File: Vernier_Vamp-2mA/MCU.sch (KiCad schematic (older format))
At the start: 9 parts

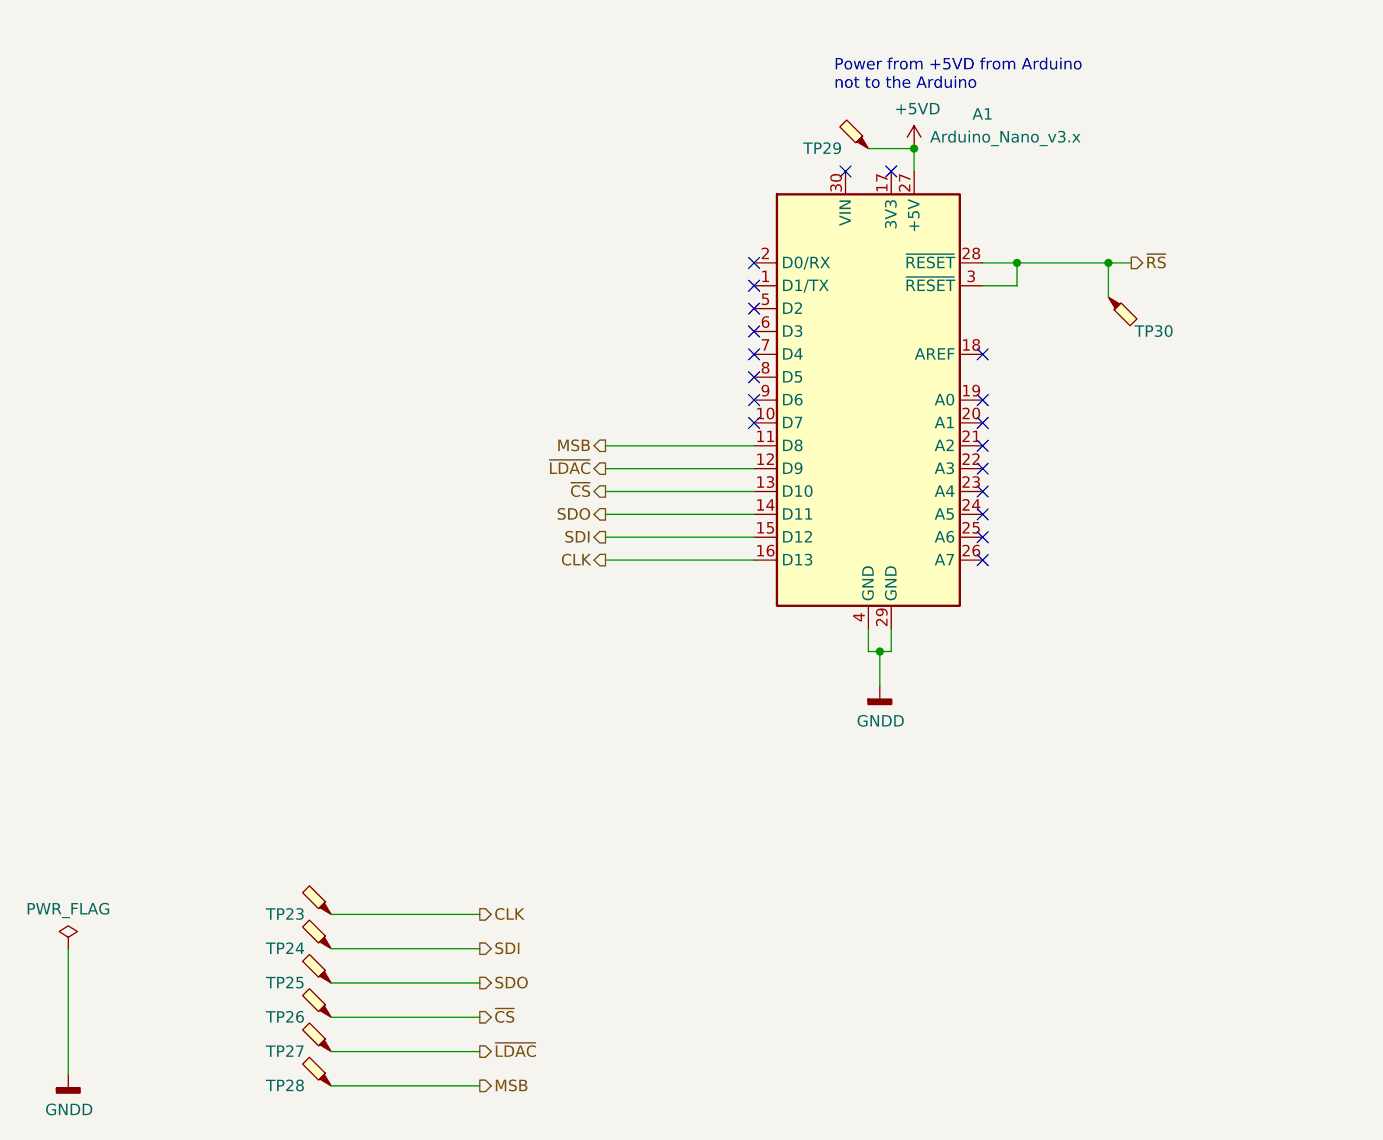
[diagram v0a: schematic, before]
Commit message: 1.0B fixes for 2mA (schematic)
Added 1.0B fixes to the 2mA version related to schematic cleanup, and addition of hysteresis and alternative way to power nano.
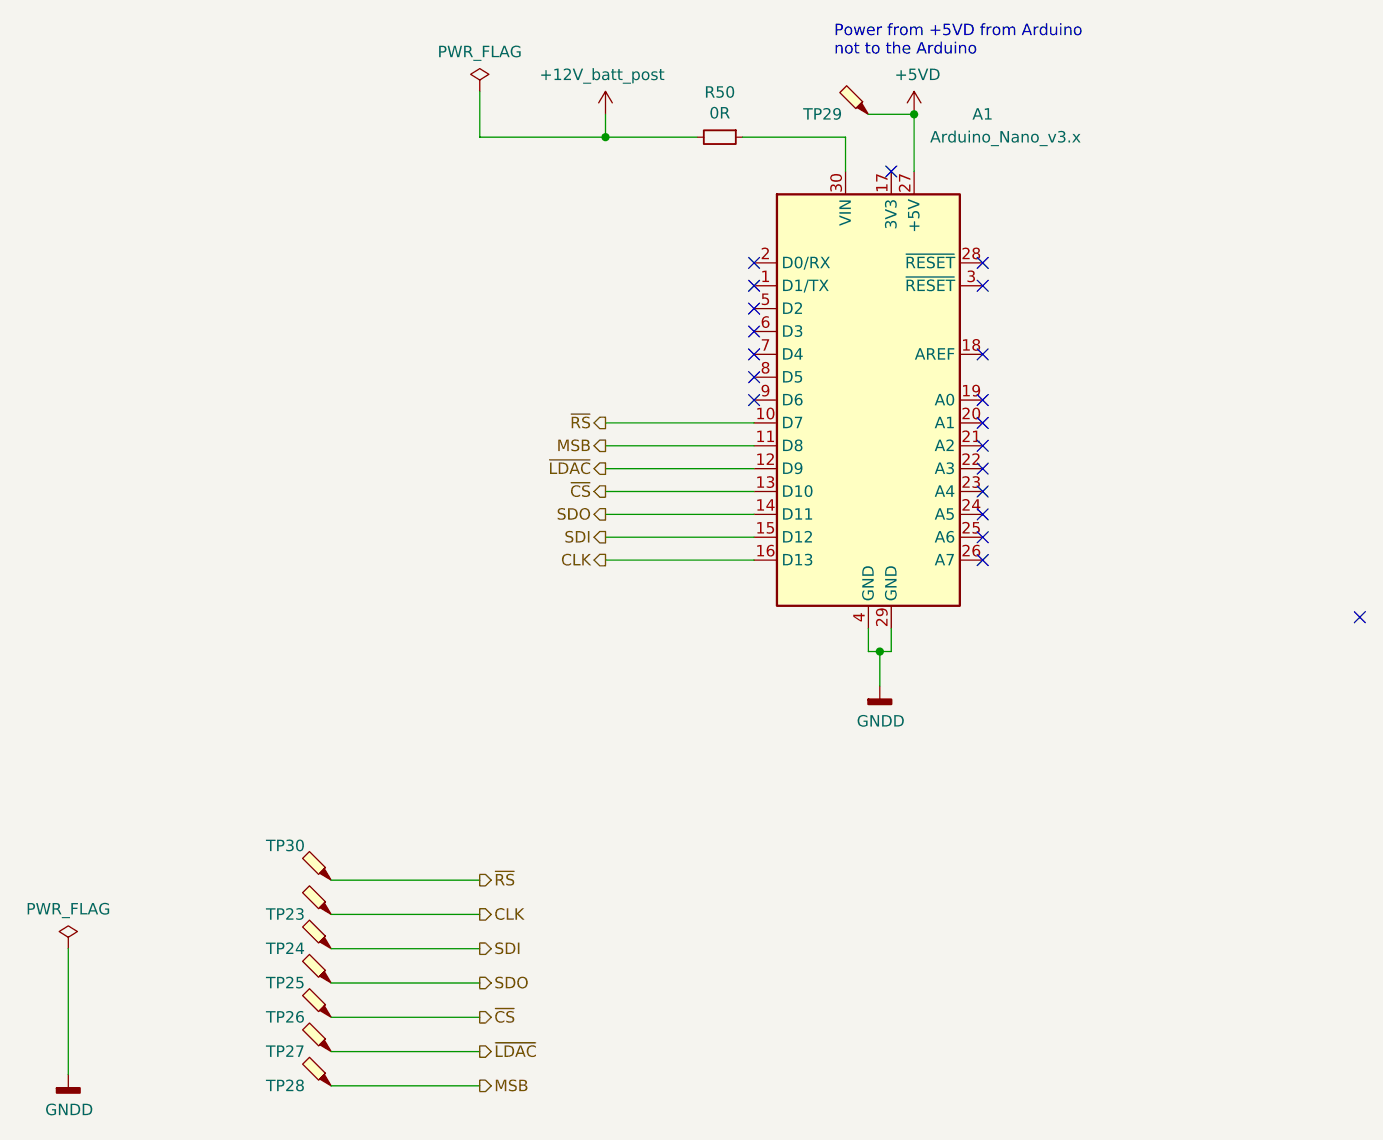
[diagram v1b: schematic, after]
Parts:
- added R50: 0R, Resistor_SMD:R_0603_1608Metric_Pad1.05x0.95mm_HandSolder, symbol Device:R_Small
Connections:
- net ~RS: now also A1.10 (D7); no longer A1.28 (~RESET), A1.3 (~RESET)
- net at A1.30 (VIN): now also R50.1
- new net +12V_batt_post: R50.2
- no-connect marks 19 -> 20
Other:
- moved on the sheet: TP29, TP30
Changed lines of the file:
@@
 $Descr A4 11693 8268
 encoding utf-8
-Sheet 4 5
-Title "\"Vernier Vamp\" Coil Driver - 200mA"
-Date "2020-02-04"
-Rev "1.0A"
+Sheet 5 7
+Title "\"Vernier Vamp\" Coil Driver - 2mA"
+Date "2020-05-05"
+Rev "1.0B"
 Comp "Strathclyde University"
 Comment1 "Designed by: Marcin Mrozowski"
@@
 Wire Wire Line
 	5350 4100 4700 4100
-Text HLabel 7000 3200 2    50   Output ~ 0
+Text HLabel 4150 5900 2    50   Output ~ 0
 ~RS
-Wire Wire Line
-	6350 3200 6500 3200
-Wire Wire Line
-	6350 3300 6500 3300
-Wire Wire Line
-	6500 3300 6500 3200
-Connection ~ 6500 3200
-Wire Wire Line
-	6500 3200 6900 3200
-NoConn ~ 5350 3900
 NoConn ~ 5350 3200
 NoConn ~ 5350 3300
@@
 	1    0    0    -1
 $EndComp
-NoConn ~ 5750 2800
 $Comp
 L power:+5VD #PWR0117
 U 1 1 610CFB70
-P 6050 2700
-F 0 "#PWR0117" H 6050 2550 50  0001 C CNN
-F 1 "+5VD" H 6065 2873 50  0000 C CNN
-F 2 "" H 6050 2700 50  0001 C CNN
-F 3 "" H 6050 2700 50  0001 C CNN
-	1    6050 2700
-	1    0    0    -1
-$EndComp
-Wire Wire Line
-	6050 2700 6050 2800
-Text Notes 5700 2450 0    50   ~ 0
+P 6050 2550
+F 0 "#PWR0117" H 6050 2400 50  0001 C CNN
+F 1 "+5VD" H 6065 2723 50  0000 C CNN
+F 2 "" H 6050 2550 50  0001 C CNN
+F 3 "" H 6050 2550 50  0001 C CNN
+	1    6050 2550
+	1    0    0    -1
+$EndComp
+Text Notes 5700 2300 0    50   ~ 0
 Power from +5VD from Arduino\nnot to the Arduino
 $Comp
@@
 L Connector:TestPoint_Probe TP30
 U 1 1 62361615
-P 6900 3350
-F 0 "TP30" V 7050 3550 50  0000 C CNN
-F 1 "TestPoint_Probe" V 7099 3405 50  0001 C CNN
-F 2 "TestPoint:TestPoint_Pad_D1.0mm" H 7100 3350 50  0001 C CNN
-F 3 "~" H 7100 3350 50  0001 C CNN
-	1    6900 3350
-	0    1    1    0
-$EndComp
-Wire Wire Line
-	6900 3350 6900 3200
-Connection ~ 6900 3200
-Wire Wire Line
-	6900 3200 7000 3200
+P 3500 5900
+F 0 "TP30" V 3650 6100 50  0000 C CNN
+F 1 "TestPoint_Probe" V 3699 5955 50  0001 C CNN
+F 2 "TestPoint:TestPoint_Pad_D1.0mm" H 3700 5900 50  0001 C CNN
+F 3 "~" H 3700 5900 50  0001 C CNN
+	1    3500 5900
+	0    -1   -1   0
+$EndComp
 $Comp
 L Connector:TestPoint_Probe TP29
 U 1 1 62363521
-P 5850 2700
-F 0 "TP29" V 5850 2900 50  0000 C CNN
-F 1 "TestPoint_Probe" V 6049 2755 50  0001 C CNN
-F 2 "TestPoint:TestPoint_Pad_D1.0mm" H 6050 2700 50  0001 C CNN
-F 3 "~" H 6050 2700 50  0001 C CNN
-	1    5850 2700
-	0    -1   -1   0
-$EndComp
-Wire Wire Line
-	6050 2700 5850 2700
-Connection ~ 6050 2700
+P 5850 2550
+F 0 "TP29" V 5850 2750 50  0000 C CNN
+F 1 "TestPoint_Probe" V 6049 2605 50  0001 C CNN
+F 2 "TestPoint:TestPoint_Pad_D1.0mm" H 6050 2550 50  0001 C CNN
+F 3 "~" H 6050 2550 50  0001 C CNN
+	1    5850 2550
+	0    -1   -1   0
+$EndComp
+Wire Wire Line
+	6050 2550 5850 2550
+Connection ~ 6050 2550
+$Comp
+L custom_power_rails:+12V_batt_post #PWR?
+U 1 1 5EE2FEC9
+P 4700 2550
+AR Path="/5E1DD6A9/5EC279B2/5EE2FEC9" Ref="#PWR?"  Part="1"
+AR Path="/5E1DEB8C/5EE2FEC9" Ref="#PWR0182"  Part="1"
+F 0 "#PWR0182" H 4700 2500 50  0001 C CNN
+F 1 "+12V_batt_post" H 4685 2723 50  0000 C CNN
+F 2 "" H 4700 2550 50  0001 C CNN
+F 3 "" H 4700 2550 50  0001 C CNN
+	1    4700 2550
+	1    0    0    -1
+$EndComp
+Wire Wire Line
+	4150 5900 3500 5900
+Text HLabel 4700 3900 0    50   Output ~ 0
+~RS
+Wire Wire Line
+	5350 3900 4700 3900
+NoConn ~ 6350 3200
+NoConn ~ 6350 3300
+NoConn ~ 8000 4750
+Wire Wire Line
+	6050 2550 6050 2800
+Wire Wire Line
+	5750 2650 5750 2800
+Wire Wire Line
+	4700 2650 4700 2550
+Wire Wire Line
+	4700 2650 5100 2650
+Wire Wire Line
+	5300 2650 5750 2650
+$Comp
+L Device:R_Small R?
+U 1 1 5EE38105
+P 5200 2650
+AR Path="/5E1DD6A9/5EE38105" Ref="R?"  Part="1"
+AR Path="/5E1DD6A9/5EC279B2/5EE38105" Ref="R?"  Part="1"
+AR Path="/5E1DEB8C/5EE38105" Ref="R50"  Part="1"
+F 0 "R50" V 5004 2650 50  0000 C CNN
+F 1 "0R" V 5095 2650 50  0000 C CNN
+F 2 "Resistor_SMD:R_0603_1608Metric_Pad1.05x0.95mm_HandSolder" H 5200 2650 50  0001 C CNN
+F 3 "~" H 5200 2650 50  0001 C CNN
+	1    5200 2650
+	0    1    1    0
+$EndComp
+$Comp
+L power:PWR_FLAG #FLG0107
+U 1 1 5F0A98D5
+P 4150 2450
+AR Path="/5E1DEB8C/5F0A98D5" Ref="#FLG0107"  Part="1"
+AR Path="/5E1DD6A9/5EC279B2/5F0A98D5" Ref="#FLG?"  Part="1"
+F 0 "#FLG0107" H 4150 2525 50  0001 C CNN
+F 1 "PWR_FLAG" H 4150 2623 50  0000 C CNN
+F 2 "" H 4150 2450 50  0001 C CNN
+F 3 "~" H 4150 2450 50  0001 C CNN
+	1    4150 2450
+	1    0    0    -1
+$EndComp
+Wire Wire Line
+	4150 2450 4150 2650
+Wire Wire Line
+	4700 2650 4150 2650
+Connection ~ 4700 2650
 $EndSCHEMATC

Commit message: Applied 1.0B changes to 2mA version
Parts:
- added TP48: TestPoint_Probe, TestPoint:TestPoint_Pad_D1.0mm, symbol Connector:TestPoint_Probe
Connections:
- net at A1.30 (VIN), R50.1: now also TP48.1
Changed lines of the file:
@@
 Wire Wire Line
 	4700 2650 5100 2650
-Wire Wire Line
-	5300 2650 5750 2650
 $Comp
 L Device:R_Small R?
@@
 L power:PWR_FLAG #FLG0107
 U 1 1 5F0A98D5
-P 4150 2450
+P 4200 2450
 AR Path="/5E1DEB8C/5F0A98D5" Ref="#FLG0107"  Part="1"
 AR Path="/5E1DD6A9/5EC279B2/5F0A98D5" Ref="#FLG?"  Part="1"
-F 0 "#FLG0107" H 4150 2525 50  0001 C CNN
-F 1 "PWR_FLAG" H 4150 2623 50  0000 C CNN
-F 2 "" H 4150 2450 50  0001 C CNN
-F 3 "~" H 4150 2450 50  0001 C CNN
-	1    4150 2450
+F 0 "#FLG0107" H 4200 2525 50  0001 C CNN
+F 1 "PWR_FLAG" H 4200 2623 50  0000 C CNN
+F 2 "" H 4200 2450 50  0001 C CNN
+F 3 "~" H 4200 2450 50  0001 C CNN
+	1    4200 2450
 	1    0    0    -1
 $EndComp
 Wire Wire Line
-	4150 2450 4150 2650
+	4200 2450 4200 2650
+Connection ~ 4700 2650
+$Comp
+L Connector:TestPoint_Probe TP48
+U 1 1 5EB89D09
+P 5450 2300
+F 0 "TP48" V 5450 2500 50  0000 C CNN
+F 1 "TestPoint_Probe" V 5649 2355 50  0001 C CNN
+F 2 "TestPoint:TestPoint_Pad_D1.0mm" H 5650 2300 50  0001 C CNN
+F 3 "~" H 5650 2300 50  0001 C CNN
+	1    5450 2300
+	0    -1   -1   0
+$EndComp
 Wire Wire Line
-	4700 2650 4150 2650
-Connection ~ 4700 2650
+	4200 2650 4700 2650
+Wire Wire Line
+	5300 2650 5450 2650
+Wire Wire Line
+	5450 2300 5450 2650
+Connection ~ 5450 2650
+Wire Wire Line
+	5450 2650 5750 2650
 $EndSCHEMATC
